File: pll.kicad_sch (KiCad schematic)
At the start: 0 parts

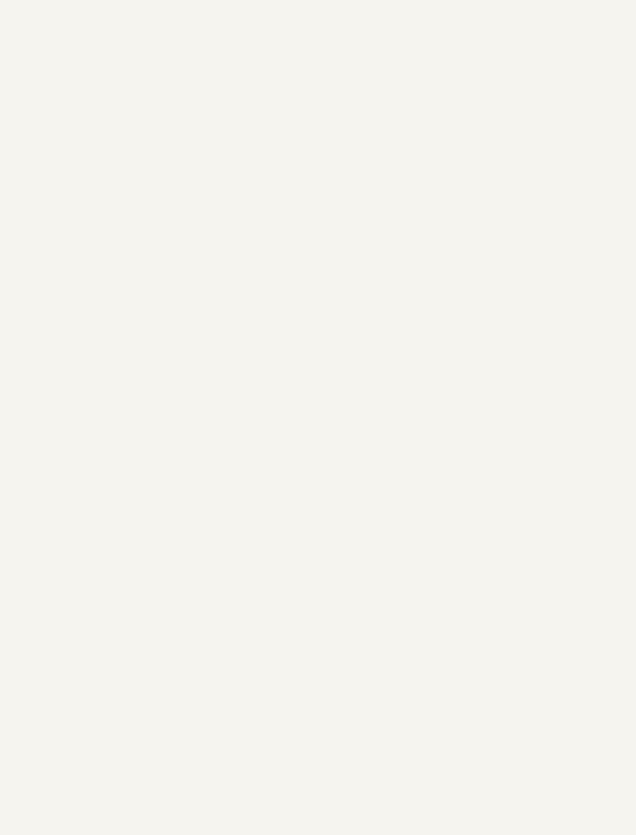
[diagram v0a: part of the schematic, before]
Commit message: Added SFP connector
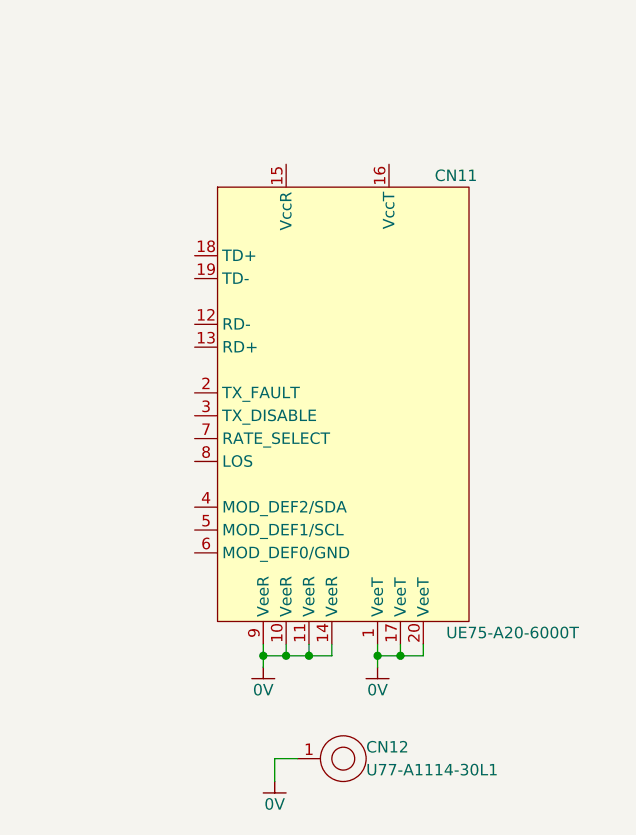
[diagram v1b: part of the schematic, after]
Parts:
- added CN11: UE75-A20-6000T, Connector_WUT:Amphenol_UE75-A20-6000T, symbol Connector_WUT:Amphenol_UE75-A20-6000T
- added CN12: U77-A1114-30L1, Connector_WUT:Amphenol_U77-A1114-30L1, symbol Connector_WUT:Amphenol_U77-A1114-30L1
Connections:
- new net 0V: CN11.1 (VeeT), CN11.10 (VeeR), CN11.11 (VeeR), CN11.14 (VeeR), CN11.17 (VeeT), CN11.20 (VeeT), CN11.9 (VeeR), CN12.1
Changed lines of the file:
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@@
 (kicad_sch (version 20230121) (generator eeschema)
   (paper "A4")
+  (junction (at 190.5 140.97) (diameter 0) (color 0 0 0 0)
+  )
+  (junction (at 177.8 140.97) (diameter 0) (color 0 0 0 0)
+  )
+  (junction (at 175.26 140.97) (diameter 0) (color 0 0 0 0)
+  )
+  (junction (at 187.96 140.97) (diameter 0) (color 0 0 0 0)
+  )
+  (junction (at 180.34 140.97) (diameter 0) (color 0 0 0 0)
+  )
+  (wire (pts (xy 180.34 140.97) (xy 182.88 140.97))
+    (stroke (width 0) (type default))
+  )
+  (wire (pts (xy 182.88 140.97) (xy 182.88 139.7))
+    (stroke (width 0) (type default))
+  )
+  (wire (pts (xy 175.26 140.97) (xy 177.8 140.97))
+    (stroke (width 0) (type default))
+  )
+  (wire (pts (xy 190.5 139.7) (xy 190.5 140.97))
+    (stroke (width 0) (type default))
+  )
+  (wire (pts (xy 177.8 140.97) (xy 180.34 140.97))
+    (stroke (width 0) (type default))
+  )
+  (wire (pts (xy 187.96 139.7) (xy 187.96 140.97))
+    (stroke (width 0) (type default))
+  )
+  (wire (pts (xy 175.26 140.97) (xy 175.26 142.24))
+    (stroke (width 0) (type default))
+  )
+  (wire (pts (xy 176.53 152.4) (xy 179.07 152.4))
+    (stroke (width 0) (type default))
+  )
+  (wire (pts (xy 180.34 139.7) (xy 180.34 140.97))
+    (stroke (width 0) (type default))
+  )
+  (wire (pts (xy 177.8 139.7) (xy 177.8 140.97))
+    (stroke (width 0) (type default))
+  )
+  (wire (pts (xy 190.5 140.97) (xy 193.04 140.97))
+    (stroke (width 0) (type default))
+  )
+  (wire (pts (xy 193.04 140.97) (xy 193.04 139.7))
+    (stroke (width 0) (type default))
+  )
+  (wire (pts (xy 187.96 140.97) (xy 187.96 142.24))
+    (stroke (width 0) (type default))
+  )
+  (wire (pts (xy 175.26 139.7) (xy 175.26 140.97))
+    (stroke (width 0) (type default))
+  )
+  (wire (pts (xy 176.53 154.94) (xy 176.53 152.4))
+    (stroke (width 0) (type default))
+  )
+  (wire (pts (xy 187.96 140.97) (xy 190.5 140.97))
+    (stroke (width 0) (type default))
+  )
+  (symbol (lib_id "Power_WUT:0V") (at 176.53 154.94 0) (unit 1)
+    (in_bom no) (on_board no) (dnp no) (fields_autoplaced)
+    (property "Reference" "#PWR0197" (at 176.53 154.94 0)
+      (effects (font (size 1.27 1.27)) hide)
+    )
+    (property "Value" "0V" (at 176.53 157.48 0) (do_not_autoplace)
+      (effects (font (size 1.27 1.27)))
+    )
+    (property "Footprint" "" (at 176.53 154.94 0)
+      (effects (font (size 1.27 1.27)) hide)
+    )
+    (property "Datasheet" "" (at 176.53 154.94 0)
+      (effects (font (size 1.27 1.27)) hide)
+    )
+    (pin "1")
+    (instances
+      (project "Master Timing Card"
+        (path "/6e8e281e-e30f-459d-852f-231836068db5/4066cd97-f2f5-4d90-9329-88af4fe2410f"
+          (reference "#PWR0197") (unit 1)
+        )
+      )
+    )
+  )
+  (symbol (lib_id "Power_WUT:0V") (at 187.96 142.24 0) (unit 1)
+    (in_bom no) (on_board no) (dnp no) (fields_autoplaced)
+    (property "Reference" "#PWR0196" (at 187.96 142.24 0)
+      (effects (font (size 1.27 1.27)) hide)
+    )
+    (property "Value" "0V" (at 187.96 144.78 0) (do_not_autoplace)
+      (effects (font (size 1.27 1.27)))
+    )
+    (property "Footprint" "" (at 187.96 142.24 0)
+      (effects (font (size 1.27 1.27)) hide)
+    )
+    (property "Datasheet" "" (at 187.96 142.24 0)
+      (effects (font (size 1.27 1.27)) hide)
+    )
+    (pin "1")
+    (instances
+      (project "Master Timing Card"
+        (path "/6e8e281e-e30f-459d-852f-231836068db5/4066cd97-f2f5-4d90-9329-88af4fe2410f"
+          (reference "#PWR0196") (unit 1)
+        )
+      )
+    )
+  )
+  (symbol (lib_id "Power_WUT:0V") (at 175.26 142.24 0) (unit 1)
+    (in_bom no) (on_board no) (dnp no) (fields_autoplaced)
+    (property "Reference" "#PWR0195" (at 175.26 142.24 0)
+      (effects (font (size 1.27 1.27)) hide)
+    )
+    (property "Value" "0V" (at 175.26 144.78 0) (do_not_autoplace)
+      (effects (font (size 1.27 1.27)))
+    )
+    (property "Footprint" "" (at 175.26 142.24 0)
+      (effects (font (size 1.27 1.27)) hide)
+    )
+    (property "Datasheet" "" (at 175.26 142.24 0)
+      (effects (font (size 1.27 1.27)) hide)
+    )
+    (pin "1")
+    (instances
+      (project "Master Timing Card"
+        (path "/6e8e281e-e30f-459d-852f-231836068db5/4066cd97-f2f5-4d90-9329-88af4fe2410f"
+          (reference "#PWR0195") (unit 1)
+        )
+      )
+    )
+  )
+  (symbol (lib_id "Connector_WUT:Amphenol_U77-A1114-30L1") (at 184.15 152.4 0) (unit 1)
+    (in_bom yes) (on_board yes) (dnp no) (fields_autoplaced)
+    (property "Reference" "CN12" (at 186.69 151.13 0) (do_not_autoplace)
+      (effects (font (size 1.27 1.27)) (justify left))
+    )
+    (property "Value" "U77-A1114-30L1" (at 186.69 153.67 0) (do_not_autoplace)
+      (effects (font (size 1.27 1.27)) (justify left))
+    )
+    (property "Footprint" "Connector_WUT:Amphenol_U77-A1114-30L1" (at 184.15 152.4 0)
+      (effects (font (size 1.27 1.27)) hide)
+    )
+    (property "Datasheet" "https://mm.digikey.com/Volume0/opasdata/d220001/medias/docus/411/U77-A111X-X0LX-RevA_Dwg.pdf" (at 184.15 152.4 0)
+      (effects (font (size 1.27 1.27)) hide)
+    )
+    (property "Manufacturer" "Amphenol ICC" (at 184.15 152.4 0)
+      (effects (font (size 1.27 1.27)) hide)
+    )
+    (property "MPN" "U77-A1114-30L1" (at 184.15 152.4 0)
+      (effects (font (size 1.27 1.27)) hide)
+    )
+    (pin "1")
+    (instances
+      (project "Master Timing Card"
+        (path "/6e8e281e-e30f-459d-852f-231836068db5/4066cd97-f2f5-4d90-9329-88af4fe2410f"
+          (reference "CN12") (unit 1)
+        )
+      )
+    )
+  )
+  (symbol (lib_id "Connector_WUT:Amphenol_UE75-A20-6000T") (at 185.42 111.76 0) (unit 1)
+    (in_bom yes) (on_board yes) (dnp no) (fields_autoplaced)
+    (property "Reference" "CN11" (at 194.31 87.63 0) (do_not_autoplace)
+      (effects (font (size 1.27 1.27)) (justify left))
+    )
+    (property "Value" "UE75-A20-6000T" (at 195.58 138.43 0) (do_not_autoplace)
+      (effects (font (size 1.27 1.27)) (justify left))
+    )
+    (property "Footprint" "Connector_WUT:Amphenol_UE75-A20-6000T" (at 170.18 109.22 0)
+      (effects (font (size 1.27 1.27)) hide)
+    )
+    (property "Datasheet" "https://mm.digikey.com/Volume0/opasdata/d220001/medias/docus/895/Ux75-A20-x00xx.pdf" (at 170.18 109.22 0)
+      (effects (font (size 1.27 1.27)) hide)
+    )
+    (property "Manufacturer" "Amphenol ICC" (at 185.42 111.76 0)
+      (effects (font (size 1.27 1.27)) hide)
+    )
+    (property "MPN" "UE75-A20-6000T" (at 185.42 111.76 0)
+      (effects (font (size 1.27 1.27)) hide)
+    )
+    (pin "1")
+    (pin "10")
+    (pin "11")
+    (pin "12")
+    (pin "13")
+    (pin "14")
+    (pin "15")
+    (pin "16")
+    (pin "17")
+    (pin "18")
+    (pin "19")
+    (pin "2")
+    (pin "20")
+    (pin "3")
+    (pin "4")
+    (pin "5")
+    (pin "6")
+    (pin "7")
+    (pin "8")
+    (pin "9")
+    (instances
+      (project "Master Timing Card"
+        (path "/6e8e281e-e30f-459d-852f-231836068db5/4066cd97-f2f5-4d90-9329-88af4fe2410f"
+          (reference "CN11") (unit 1)
+        )
+      )
+    )
+  )
   (sheet (at 82.55 17.78) (size 38.1 21.59) (fields_autoplaced)
     (stroke (width 0.1524) (type solid))

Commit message: Schematic mostly done
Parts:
- added C109, C110, C112: 100p, Capacitor_SMD:C_0402_1005Metric, symbol Auto_Library_WUT:Kemet C0402C101F1GACTU
- added C13: 15p, Capacitor_SMD:C_0402_1005Metric, symbol Auto_Library_WUT:Kemet C0402C150D5GACTU
- added C15, C17, C7 (x3): 10u, Capacitor_SMD:C_0603_1608Metric, symbol Auto_Library_WUT:Samsung Electro-Mechanics CL10A106MO8NQNC
- added C157, C35, C9 (x5): 100n, Capacitor_SMD:C_0402_1005Metric, symbol Auto_Library_WUT:Yageo CC0402KRX7R8BB104
- added CN15: 731385033, Connector_WUT:BNC_Molex_731385033, symbol Connector_WUT:BNC_Molex_731385033
- added D9: 5V0, Diode_SMD:D_SOD-523, symbol Auto_Library_WUT:Littelfuse AQ3522-01LTG
- added FB26, FB27: 600R, Inductor_SMD:L_0603_1608Metric, symbol Auto_Library_WUT:Murata BLM18AG601SN1D
- added L5, L6: 1u0, Inductor_SMD:L_0603_1608Metric, symbol Auto_Library_WUT:Coilcraft 0603AF-102XJR
- added LD8: Green, LED_SMD:LED_0603_1608Metric, symbol Auto_Library_WUT:Ekinglux_E6C0603VGAC1UDA
- added Q6: DMN62D0U-7, Package_TO_SOT_SMD:SOT-23, symbol FET_WUT:DMN62D0U-7
- added R100, R101, R105, R106, R110, R111: 33R, Resistor_SMD:R_0402_1005Metric, symbol Auto_Library_WUT:KOA Speer RK73H1ETTP33R0F
- added R102, R107, R112: 140R, Resistor_SMD:R_0402_1005Metric, symbol Auto_Library_WUT:KOA Speer RK73H1ETTP1400F
- added R103, R104, R108, R109, R113, R114: 180R, Resistor_SMD:R_0402_1005Metric, symbol Auto_Library_WUT:KOA Speer RK73H1ETTP1800F
- added R118, R129: 10k, Resistor_SMD:R_0402_1005Metric, symbol Auto_Library_WUT:KOA Speer RK73H1ETTP1002F
- added R20: 22k, Resistor_SMD:R_0402_1005Metric, symbol Auto_Library_WUT:KOA Speer RK73H1ETTP2202F
- added R21: 13k, Resistor_SMD:R_0402_1005Metric, symbol Auto_Library_WUT:KOA Speer RK73H1ETTP1302F
- added R89: 100R, Resistor_SMD:R_0402_1005Metric, symbol Auto_Library_WUT:KOA Speer RK73H1ETTP1000F
- added R90, R91, R92, R93: 49R9, Resistor_SMD:R_0402_1005Metric, symbol Auto_Library_WUT:KOA Speer RK73H1ETTP49R9F
- added R94: 475R, Resistor_SMD:R_0402_1005Metric, symbol Auto_Library_WUT:KOA Speer RK73H1ETTP4750F
- added R95, R96: 10R, Resistor_SMD:R_0402_1005Metric, symbol Auto_Library_WUT:KOA Speer RK73H1ETTP10R0F
- added R97, R98: 20R, Resistor_SMD:R_0402_1005Metric, symbol Auto_Library_WUT:KOA Speer RK73H1ETTP20R0F
- added R99: 51R, Resistor_SMD:R_0402_1005Metric, symbol Auto_Library_WUT:KOA Speer RK73H1ETTP51R0F
- added T4: TC2-72T+, RF_WUT:MiniCircuits_AT1521, symbol Transformer_WUT:Minicircuits_TC2-72T
- added TP1, TP4: ~, TestPoint:TestPoint_Pad_D1.0mm, symbol Layout_WUT:TestPoint_1mm_SMD
- added U11: SY75576LKY, Package_SO:TSSOP-20_4.4x6.5mm_P0.65mm, symbol IC_WUT:Microchip_SY75576LKY
- added U15: SN74LVC1G02DCK, Package_TO_SOT_SMD:SOT-353_SC-70-5, symbol Logic_WUT:TI_SN74LVC1G02DCKR
- added U3: TI TPS79301DBV, Package_TO_SOT_SMD:SOT-23-6, symbol IC_WUT:TI_TPS79301DBV
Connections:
- net 0V: now also C109.2, C110.2, C112.2, C15.2, C157.2, C17.2, C35.1, C7.2, C7.2, C7.2, C9.2, C9.2, C9.2, C9.2, C9.2, CN15.2 (Ext), D9.2 (A), LD8.1 (K), Q6.2 (S), R103.2, R104.1, R108.1, R109.2, R113.1, R114.2, R118.2, R21.2, R90.2, R91.2, R92.2, R93.2, R94.2, R99.2, T4.6, U11.16 (GND), U11.9 (GND), U15.3 (0V), U3.2 (GND)
- net Frequency Synthesiser 1/~{PLL_LOCK_OD}: now also U15.1
- net Frequency Synthesiser 2/~{PLL_LOCK_OD}: now also U15.2
- net at CN11.12 (RD-): now also R95.2
- net at CN11.13 (RD+): now also R96.2
- net at CN11.15 (VccR): now also C7.1, C9.1, L5.2
- net at CN11.16 (VccT): now also C9.1, L6.2
- net SFP_TX_P: now reaches CN11.18 (TD+)
- net SFP_TX_P: now also R100.2, R102.1, R104.2
- net SFP_TX_N: now reaches CN11.19 (TD-)
- net SFP_TX_N: now also R101.2, R102.2, R103.1
- net SFP_TX_FAULT_OD: now reaches CN11.2 (TX_FAULT)
- net at CN11.3 (TX_DISABLE): now also Q6.3 (D)
- net SFP_SDA: now reaches CN11.4 (MOD_DEF2/SDA)
- net SFP_SDA: now also C112.1
- net SFP_SCL: now reaches CN11.5 (MOD_DEF1/SCL)
- net SFP_SCL: now also C110.1
- net ~{SFP_PRESENT}: now reaches CN11.6 (MOD_DEF0/GND)
- net ~{SFP_PRESENT}: now also C109.1
- net at CN11.7 (RATE_SELECT): now also TP4.1
- net SFP_LOS_OD: now reaches CN11.8 (LOS)
- new net: R110.1, U11.14 (CLKC_P)
- new net: C35.2, T4.2
- new net: C13.1, C15.1, C17.1, R20.1, TP1.1, U11.15 (VDD), U11.2 (VDDIN), U3.6 (OUT)
- new net: LD8.2 (A), R129.1
- new net: R93.1, U11.3 (IN1_P)
- new net: C7.1, FB26.2, U3.1 (IN), U3.3 (EN)
- new net: R94.1, U11.10 (IREF)
- new net: R89.2, T4.1, U11.11 (CLKD_N)
- new net: R89.1, T4.3, U11.12 (CLKD_P)
- new net: R111.1, U11.13 (CLKC_N)
- new net: R106.1, U11.17 (CLKB_N)
- new net: R105.1, U11.18 (CLKB_P)
- new net: R101.1, U11.19 (CLKA_N)
- new net: R100.1, U11.20 (CLKA_P)
- new net: R90.1, U11.4 (IN1_N)
- new net: R97.1, T4.4
- new net: C7.1, C9.1, FB27.2, L5.1, L6.1
- new net: C13.2, R20.2, R21.1, U3.5 (FB)
- new net: CN15.1 (In), D9.1 (K), R98.2
- new net: R97.2, R98.1, R99.1
- new net: C9.1, U3.4 (NR)
- new net 3V3: C157.1, FB27.1, U15.5 (VCC)
- new net 5V0_PI: FB26.1
- new net PLL1_CLK_N: R106.2, R107.2, R109.1
- new net PLL1_CLK_P: R105.2, R107.1, R108.2
- new net PLL2_CLK_N: R111.2, R112.2, R114.1
- new net PLL2_CLK_P: R110.2, R112.1, R113.2
- new net PLL_LOCK: R129.2, U15.4
- new net SFP_REFCLK_N: R92.1, R96.1, U11.7 (IN2_N)
- new net SFP_REFCLK_P: R91.1, R95.1, U11.6 (IN2_P)
- new net SFP_TX_DISABLE: C9.1, Q6.1 (G), R118.1
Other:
- note added: "Either fit this resistor or components for additonal 10MHz out"
- note added: "I2C Address = 0x50"
- note added: "Place resistors close to buffer IC"
- note added: "Should be 0.7V amplitude = 5mW 7.5dB attenuator to give just under 0dBm"
- note added: "TODO Backup oscillator"
- note added: "TODO GPS IN"
- note added: "TODO U11 GPIO"
- note added: "Vfb = 1.225V Vout = 1.225 * (1+22/13) = 3.30V"
- moved on the sheet: CN12

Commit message: schematic complete
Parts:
- removed R90, R93: 49R9, Resistor_SMD:R_0402_1005Metric, symbol Auto_Library_WUT:KOA Speer RK73H1ETTP49R9F
- added C159: 100n, Capacitor_SMD:C_0402_1005Metric, symbol Auto_Library_WUT:Yageo CC0402KRX7R8BB104
- added R137: 10k, Resistor_SMD:R_0402_1005Metric, symbol Auto_Library_WUT:KOA Speer RK73H1ETTP1002F
- added R90: 100R, Resistor_SMD:R_0402_1005Metric, symbol Auto_Library_WUT:KOA Speer RK73H1ETTP1000F
- U15: symbol Logic_WUT:TI_SN74LVC1G02DCKR -> Logic_WUT:TI_SN74LVC1G02DCK
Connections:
- net 0V: now also C159.2, R137.2
- net REF_CLK_P: now reaches U11.3 (IN1_P)
- net REF_CLK_P: now also R90.1
- net CLK_SEL: now reaches U11.1 (SEL)
- net CLK_SEL: now also C159.1, R137.1
- net REF_CLK_N: now reaches U11.4 (IN1_N)
- net REF_CLK_N: now also R90.2
- no-connect marks 0 -> 2
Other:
- note added: "Internal pullups"
- note removed: "TODO Backup oscillator"
- note removed: "TODO GPS IN"
- note removed: "TODO U11 GPIO"
- moved on the sheet: R91, R92
